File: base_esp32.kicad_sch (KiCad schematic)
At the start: 3 parts, among them J1 Input Source, U1 LM7805_TO220, U2 ESP32-DevKitC

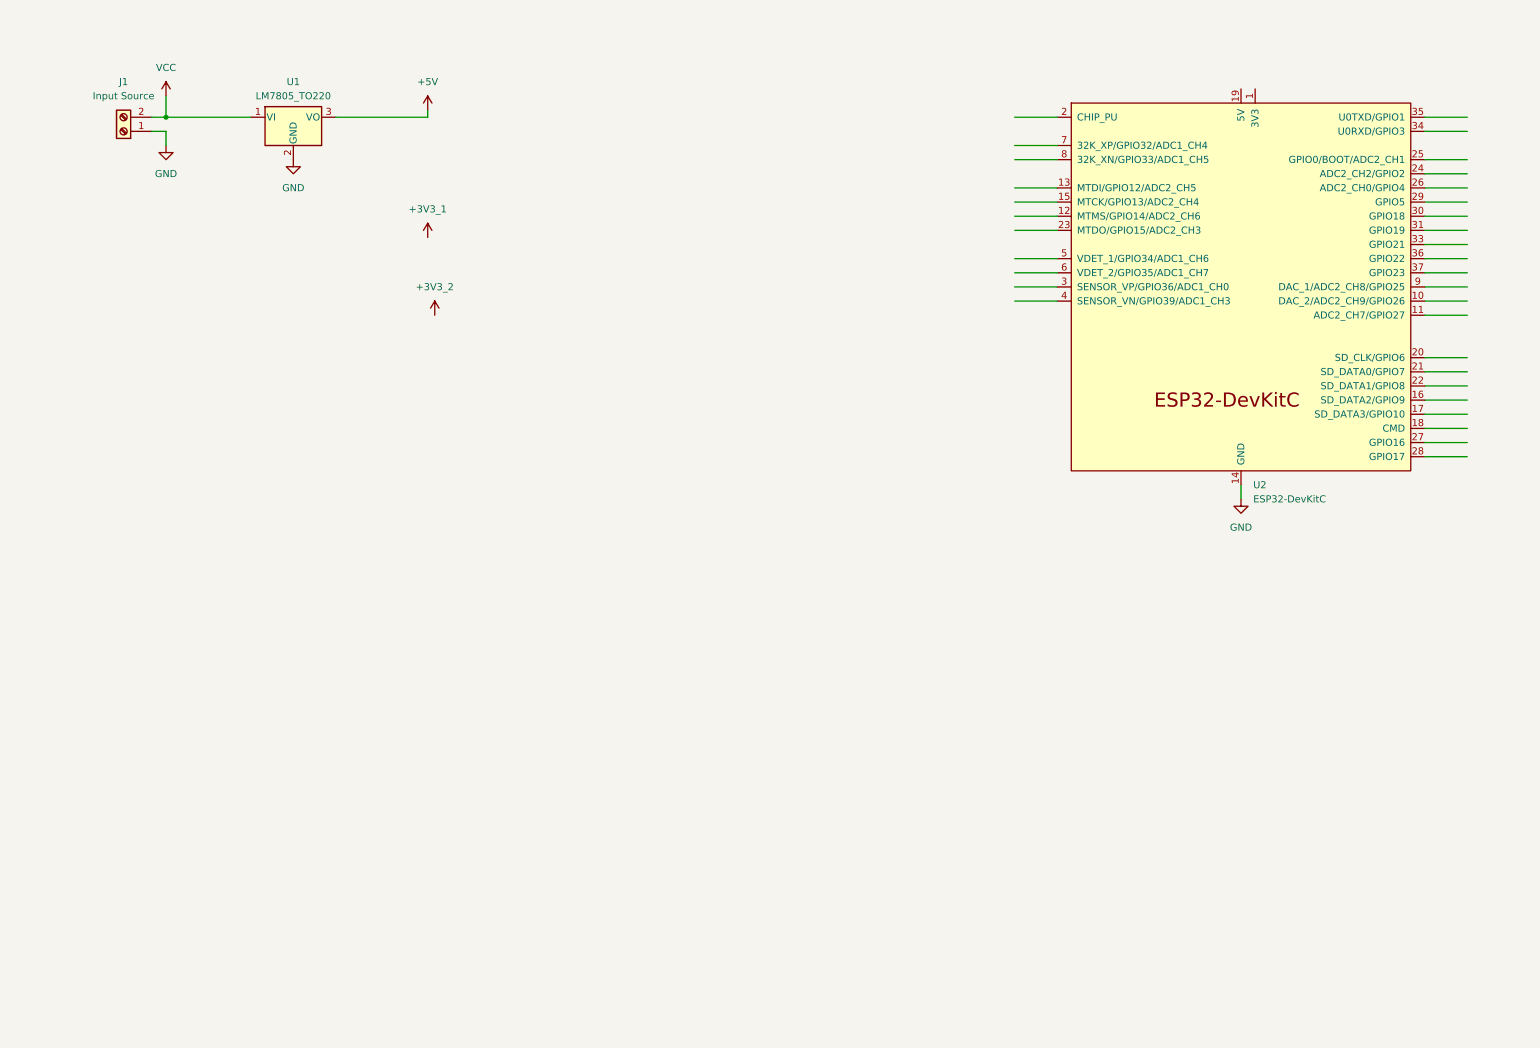
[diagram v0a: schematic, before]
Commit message: add: schematic
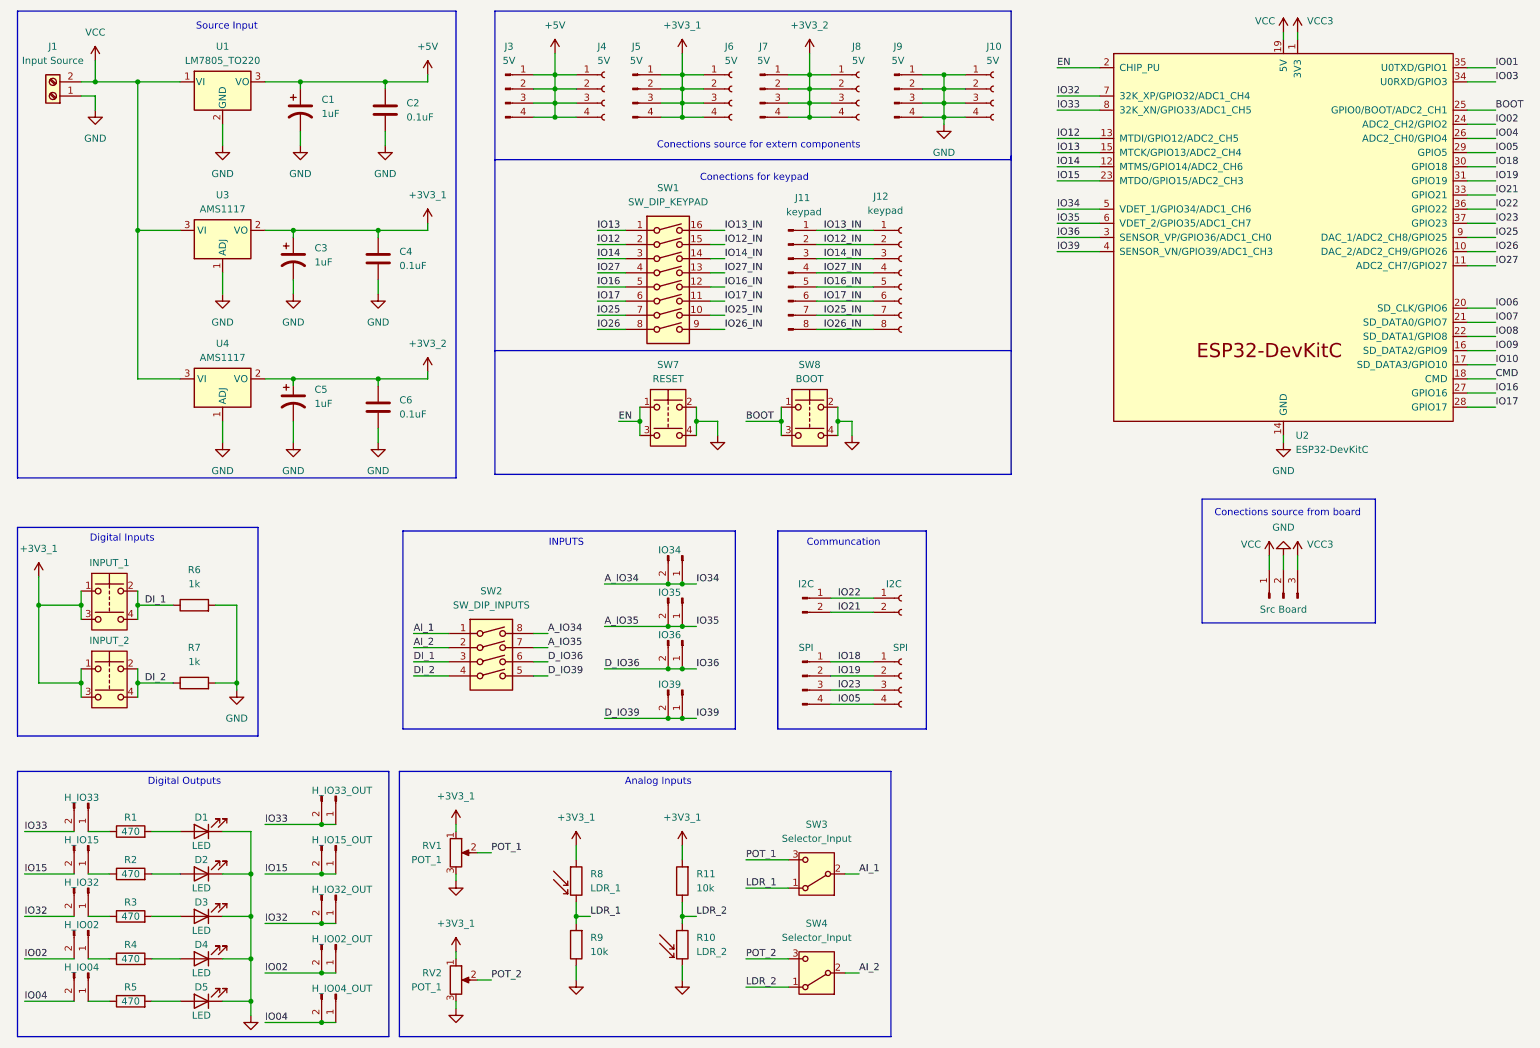
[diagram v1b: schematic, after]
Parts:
- added C1, C3, C5: 1uF, symbol Device:C_Polarized_US
- added C2, C4, C6: 0.1uF, symbol Device:C
- added D1, D2, D3, D4, D5: LED, symbol Device:LED
- added J10, J4, J6, J8: 5V, symbol Connector:Conn_01x04_Socket
- added J11: keypad, symbol Connector:Conn_01x08_Pin
- added J12: keypad, symbol Connector:Conn_01x08_Socket
- added J13: H_IO33, symbol Connector:Conn_01x02_Pin
- added J14: H_IO15, symbol Connector:Conn_01x02_Pin
- added J15: H_IO32, symbol Connector:Conn_01x02_Pin
- added J16: H_IO02, symbol Connector:Conn_01x02_Pin
- added J17: H_IO04, symbol Connector:Conn_01x02_Pin
- added J18: H_IO33_OUT, symbol Connector:Conn_01x02_Pin
- added J19: H_IO15_OUT, symbol Connector:Conn_01x02_Pin
- added J2: Src Board, symbol Connector:Conn_01x03_Pin
- added J20: H_IO32_OUT, symbol Connector:Conn_01x02_Pin
- added J21: H_IO02_OUT, symbol Connector:Conn_01x02_Pin
- added J22: H_IO04_OUT, symbol Connector:Conn_01x02_Pin
- added J23: I2C, symbol Connector:Conn_01x02_Pin
- added J24: I2C, symbol Connector:Conn_01x02_Socket
- added J25: SPI, symbol Connector:Conn_01x04_Pin
- added J26: SPI, symbol Connector:Conn_01x04_Socket
- added J27: IO34, symbol Connector:Conn_01x02_Pin
- added J28: IO35, symbol Connector:Conn_01x02_Pin
- added J29: IO36, symbol Connector:Conn_01x02_Pin
- added J3, J5, J7, J9: 5V, symbol Connector:Conn_01x04_Pin
- added J30: IO39, symbol Connector:Conn_01x02_Pin
- added R1, R2, R3, R4, R5: 470, symbol Device:R
- added R10: LDR_2, OptoDevice:R_LDR_5.0x4.1mm_P3mm_Vertical, symbol Sensor_Optical:A9013
- added R11, R9: 10k, symbol Device:R
- added R6, R7: 1k, symbol Device:R
- added R8: LDR_1, OptoDevice:R_LDR_5.0x4.1mm_P3mm_Vertical, symbol Sensor_Optical:A9013
- added RV1, RV2: POT_1, symbol Device:R_Potentiometer
- added SW1: SW_DIP_KEYPAD, symbol Switch:SW_DIP_x08
- added SW2: SW_DIP_INPUTS, symbol Switch:SW_DIP_x04
- added SW3, SW4: Selector_Input, symbol Switch:SW_SPDT
- added SW5: INPUT_1, symbol Switch:SW_Push_Dual
- added SW6: INPUT_2, symbol Switch:SW_Push_Dual
- added SW7: RESET, symbol Switch:SW_Push_Dual
- added SW8: BOOT, symbol Switch:SW_Push_Dual
- added U3, U4: AMS1117, Package_TO_SOT_SMD:SOT-223-3_TabPin2, symbol Regulator_Linear:AMS1117
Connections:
- net +3V3_1: now also C3.1, C4.1, J5.1 (Pin_1), J5.2 (Pin_2), J5.3 (Pin_3), J5.4 (Pin_4), J6.1 (Pin_1), J6.2 (Pin_2), J6.3 (Pin_3), J6.4 (Pin_4), R11.2, R8.1, RV1.1, RV2.1, SW5.1, SW5.3, SW6.1, SW6.3, U3.2 (VO)
- net +3V3_2: now also C5.1, C6.1, J7.1 (Pin_1), J7.2 (Pin_2), J7.3 (Pin_3), J7.4 (Pin_4), J8.1 (Pin_1), J8.2 (Pin_2), J8.3 (Pin_3), J8.4 (Pin_4), U4.2 (VO)
- net +5V: now also C1.1, C2.1, J3.1 (Pin_1), J3.2 (Pin_2), J3.3 (Pin_3), J3.4 (Pin_4), J4.1 (Pin_1), J4.2 (Pin_2), J4.3 (Pin_3), J4.4 (Pin_4)
- net GND: now also C1.2, C2.2, C3.2, C4.2, C5.2, C6.2, D1.1 (K), D2.1 (K), D3.1 (K), D4.1 (K), D5.1 (K), J10.1 (Pin_1), J10.2 (Pin_2), J10.3 (Pin_3), J10.4 (Pin_4), J2.2 (Pin_2), J9.1 (Pin_1), J9.2 (Pin_2), J9.3 (Pin_3), J9.4 (Pin_4), R10.2, R6.2, R7.2, R9.1, RV1.3, RV2.3, SW7.2, SW7.4, SW8.2, SW8.4, U3.1 (ADJ), U4.1 (ADJ)
- net VCC: now also U2.19 (5V), J2.1 (Pin_1), U3.3 (VI), U4.3 (VI)
- net VCC3: now reaches U2.1 (3V3)
- net VCC3: now also J2.3 (Pin_3)
- net IO26: now reaches U2.10 (DAC_2/ADC2_CH9/GPIO26)
- net IO26: now also SW1.8
- net IO27: now reaches U2.11 (ADC2_CH7/GPIO27)
- net IO27: now also SW1.4
- net IO14: now reaches U2.12 (MTMS/GPIO14/ADC2_CH6)
- net IO14: now also SW1.3
- net IO12: now reaches U2.13 (MTDI/GPIO12/ADC2_CH5)
- net IO12: now also SW1.2
- net IO13: now reaches U2.15 (MTCK/GPIO13/ADC2_CH4)
- net IO13: now also SW1.1
- net IO09: now reaches U2.16 (SD_DATA2/GPIO9)
- net IO10: now reaches U2.17 (SD_DATA3/GPIO10)
- net CMD: now reaches U2.18 (CMD)
- net EN: now reaches U2.2 (CHIP_PU)
- net EN: now also SW7.1, SW7.3
- net IO06: now reaches U2.20 (SD_CLK/GPIO6)
- net IO07: now reaches U2.21 (SD_DATA0/GPIO7)
- net IO08: now reaches U2.22 (SD_DATA1/GPIO8)
- net IO15: now reaches U2.23 (MTDO/GPIO15/ADC2_CH3)
- net IO15: now also J14.2 (Pin_2), J19.1 (Pin_1), J19.2 (Pin_2)
- net IO02: now reaches U2.24 (ADC2_CH2/GPIO2)
- net IO02: now also J16.2 (Pin_2), J21.1 (Pin_1), J21.2 (Pin_2)
- net BOOT: now reaches U2.25 (GPIO0/BOOT/ADC2_CH1)
- net BOOT: now also SW8.1, SW8.3
- net IO04: now reaches U2.26 (ADC2_CH0/GPIO4)
- net IO04: now also J17.2 (Pin_2), J22.1 (Pin_1), J22.2 (Pin_2)
- net IO16: now reaches U2.27 (GPIO16)
- net IO16: now also SW1.5
- net IO17: now reaches U2.28 (GPIO17)
- net IO17: now also SW1.6
- net IO05: now reaches U2.29 (GPIO5)
- net IO05: now also J25.4 (Pin_4), J26.4 (Pin_4)
- net D_IO36: now reaches U2.3 (SENSOR_VP/GPIO36/ADC1_CH0)
- net D_IO36: now also J29.1 (Pin_1), J29.2 (Pin_2), SW2.6
- net IO18: now reaches U2.30 (GPIO18)
- net IO18: now also J25.1 (Pin_1), J26.1 (Pin_1)
- net IO19: now reaches U2.31 (GPIO19)
- net IO19: now also J25.2 (Pin_2), J26.2 (Pin_2)
- net IO21: now reaches U2.33 (GPIO21)
- net IO21: now also J23.2 (Pin_2), J24.2 (Pin_2)
- net IO03: now reaches U2.34 (U0RXD/GPIO3)
- net IO01: now reaches U2.35 (U0TXD/GPIO1)
- net IO22: now reaches U2.36 (GPIO22)
- net IO22: now also J23.1 (Pin_1), J24.1 (Pin_1)
- net IO23: now reaches U2.37 (GPIO23)
- net IO23: now also J25.3 (Pin_3), J26.3 (Pin_3)
- net D_IO39: now reaches U2.4 (SENSOR_VN/GPIO39/ADC1_CH3)
- net D_IO39: now also J30.1 (Pin_1), J30.2 (Pin_2), SW2.5
- net A_IO34: now reaches U2.5 (VDET_1/GPIO34/ADC1_CH6)
- net A_IO34: now also J27.1 (Pin_1), J27.2 (Pin_2), SW2.8
- net A_IO35: now reaches U2.6 (VDET_2/GPIO35/ADC1_CH7)
- net A_IO35: now also J28.1 (Pin_1), J28.2 (Pin_2), SW2.7
- net IO32: now reaches U2.7 (32K_XP/GPIO32/ADC1_CH4)
- net IO32: now also J15.2 (Pin_2), J20.1 (Pin_1), J20.2 (Pin_2)
- net IO33: now reaches U2.8 (32K_XN/GPIO33/ADC1_CH5)
- net IO33: now also J13.2 (Pin_2), J18.1 (Pin_1), J18.2 (Pin_2)
- net IO25: now reaches U2.9 (DAC_1/ADC2_CH8/GPIO25)
- net IO25: now also SW1.7
- new net: J14.1 (Pin_1), R2.1
- new net: D3.2 (A), R3.2
- new net: J15.1 (Pin_1), R3.1
- new net: J13.1 (Pin_1), R1.1
- new net: D1.2 (A), R1.2
- new net: D2.2 (A), R2.2
- new net: D5.2 (A), R5.2
- new net: J17.1 (Pin_1), R5.1
- new net: D4.2 (A), R4.2
- new net: J16.1 (Pin_1), R4.1
- new net AI_1: SW2.1, SW3.2 (B)
- new net AI_2: SW2.2, SW4.2 (B)
- new net DI_1: R6.1, SW2.3, SW5.2, SW5.4
- new net DI_2: R7.1, SW2.4, SW6.2, SW6.4
- new net IO12_IN: J11.2 (Pin_2), J12.2 (Pin_2), SW1.15
- new net IO13_IN: J11.1 (Pin_1), J12.1 (Pin_1), SW1.16
- new net IO14_IN: J11.3 (Pin_3), J12.3 (Pin_3), SW1.14
- new net IO16_IN: J11.5 (Pin_5), J12.5 (Pin_5), SW1.12
- new net IO17_IN: J11.6 (Pin_6), J12.6 (Pin_6), SW1.11
- new net IO25_IN: J11.7 (Pin_7), J12.7 (Pin_7), SW1.10
- new net IO26_IN: J11.8 (Pin_8), J12.8 (Pin_8), SW1.9
- new net IO27_IN: J11.4 (Pin_4), J12.4 (Pin_4), SW1.13
- new net LDR_1: R8.2, R9.2, SW3.1 (A)
- new net LDR_2: R10.1, R11.1, SW4.1 (A)
- new net POT_1: RV1.2, SW3.3 (C)
- new net POT_2: RV2.2, SW4.3 (C)
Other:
- note added: "Analog Inputs"
- note added: "Communcation"
- note added: "Conections for keypad"
- note added: "Conections source for extern components"
- note added: "Conections source from board"
- note added: "Digital Inputs"
- note added: "Digital Outputs"
- note added: "INPUTS"
- note added: "Source Input"
- company: (none) -> Xizuth
- title: (none) -> Base for ESP32
- moved on the sheet: J1, U1, U2

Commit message: add: bypass source
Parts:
- added J31: bypass, symbol Connector:Conn_01x02_Pin
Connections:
- net +5V: now also J31.2 (Pin_2)
- net VCC: now also J31.1 (Pin_1)
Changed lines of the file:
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@@
 	(wire
 		(pts
+			(xy 22.86 55.88) (xy 25.4 55.88)
+		)
+		(stroke
+			(width 0)
+			(type default)
+		)
+	)
+	(wire
+		(pts
 			(xy 132.08 20.32) (xy 132.08 24.13)
 		)
@@
 	(wire
 		(pts
+			(xy 22.86 52.07) (xy 22.86 55.88)
+		)
+		(stroke
+			(width 0)
+			(type default)
+		)
+	)
+	(wire
+		(pts
 			(xy 156.21 69.85) (xy 166.37 69.85)
 		)
@@
 	(wire
 		(pts
+			(xy 21.59 52.07) (xy 22.86 52.07)
+		)
+		(stroke
+			(width 0)
+			(type default)
+		)
+	)
+	(wire
+		(pts
 			(xy 113.03 175.26) (xy 115.57 175.26)
 		)
@@
 	(wire
 		(pts
+			(xy 21.59 49.53) (xy 25.4 49.53)
+		)
+		(stroke
+			(width 0)
+			(type default)
+		)
+	)
+	(wire
+		(pts
 			(xy 175.26 29.21) (xy 179.07 29.21)
 		)
@@
 	)
 	(symbol
+		(lib_id "Connector:Conn_01x02_Pin")
+		(at 16.51 49.53 0)
+		(unit 1)
+		(exclude_from_sim no)
+		(in_bom yes)
+		(on_board yes)
+		(dnp no)
+		(property "Reference" "J31"
+			(at 17.145 44.45 0)
+			(effects
+				(font
+					(size 1.27 1.27)
+				)
+				(hide yes)
+			)
+		)
+		(property "Value" "bypass"
+			(at 19.05 46.228 0)
+			(effects
+				(font
+					(size 1.27 1.27)
+				)
+			)
+		)
+		(property "Footprint" ""
+			(at 16.51 49.53 0)
+			(effects
+				(font
+					(size 1.27 1.27)
+				)
+				(hide yes)
+			)
+		)
+		(property "Datasheet" "~"
+			(at 16.51 49.53 0)
+			(effects
+				(font
+					(size 1.27 1.27)
+				)
+				(hide yes)
+			)
+		)
+		(property "Description" "Generic connector, single row, 01x02, script generated"
+			(at 16.51 49.53 0)
+			(effects
+				(font
+					(size 1.27 1.27)
+				)
+				(hide yes)
+			)
+		)
+		(pin "1"
+		)
+		(pin "2"
+		)
+		(instances
+			(project ""
+				(path "/21b771cb-d347-44fd-932f-803ba77af901"
+					(reference "J31")
+					(unit 1)
+				)
+			)
+		)
+	)
+	(symbol
 		(lib_id "Switch:SW_SPDT")
 		(at 156.21 167.64 180)
@@
 	)
 	(symbol
+		(lib_id "power:+5V")
+		(at 25.4 55.88 0)
+		(unit 1)
+		(exclude_from_sim no)
+		(in_bom yes)
+		(on_board yes)
+		(dnp no)
+		(fields_autoplaced yes)
+		(property "Reference" "#PWR039"
+			(at 25.4 59.69 0)
+			(effects
+				(font
+					(size 1.27 1.27)
+				)
+				(hide yes)
+			)
+		)
+		(property "Value" "+5V"
+			(at 25.4 50.8 0)
+			(effects
+				(font
+					(size 1.27 1.27)
+				)
+			)
+		)
+		(property "Footprint" ""
+			(at 25.4 55.88 0)
+			(effects
+				(font
+					(size 1.27 1.27)
+				)
+				(hide yes)
+			)
+		)
+		(property "Datasheet" ""
+			(at 25.4 55.88 0)
+			(effects
+				(font
+					(size 1.27 1.27)
+				)
+				(hide yes)
+			)
+		)
+		(property "Description" "Power symbol creates a global label with name \"+5V\""
+			(at 25.4 55.88 0)
+			(effects
+				(font
+					(size 1.27 1.27)
+				)
+				(hide yes)
+			)
+		)
+		(pin "1"
+		)
+		(instances
+			(project "base_esp32"
+				(path "/21b771cb-d347-44fd-932f-803ba77af901"
+					(reference "#PWR039")
+					(unit 1)
+				)
+			)
+		)
+	)
+	(symbol
 		(lib_id "power:GND")
 		(at 240.03 90.17 0)
@@
 					(unit 1)
 				)
+			)
+		)
+	)
+	(symbol
+		(lib_id "power:VCC")
+		(at 25.4 49.53 0)
+		(unit 1)
+		(exclude_from_sim no)
+		(in_bom yes)
+		(on_board yes)
+		(dnp no)
+		(fields_autoplaced yes)
+		(property "Reference" "#PWR038"
+			(at 25.4 53.34 0)
+			(effects
+				(font
+					(size 1.27 1.27)
+				)
+				(hide yes)
+			)
+		)
+		(property "Value" "VCC"
+			(at 25.4 44.45 0)
+			(effects
+				(font
+					(size 1.27 1.27)
+				)
+			)
+		)
+		(property "Footprint" ""
+			(at 25.4 49.53 0)
+			(effects
+				(font
+					(size 1.27 1.27)
+				)
+				(hide yes)
+			)
+		)
+		(property "Datasheet" ""
+			(at 25.4 49.53 0)
+			(effects
+				(font
+					(size 1.27 1.27)
+				)
+				(hide yes)
+			)
+		)
+		(property "Description" "Power symbol creates a global label with name \"VCC\""
+			(at 25.4 49.53 0)
+			(effects
+				(font
+					(size 1.27 1.27)
+				)
+				(hide yes)
+			)
+		)
+		(pin "1"
+		)
+		(instances
+			(project "base_esp32"
+				(path "/21b771cb-d347-44fd-932f-803ba77af901"
+					(reference "#PWR038")
+					(unit 1)
+				)
